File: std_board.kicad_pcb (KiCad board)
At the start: 2 copper layers, 99.1 x 99.1 mm, 191 parts, among them IC1 ESP32, IC2 ACS712, IC3 L78L05, IC4 AMS1117-V, J1 Jumper, J10 J_DHT11, J11 Jumper, J12 Jumper, J13 J_PRess, J14 Jumper, J15 Jumper, J16 J_PRess, J17 Jumper, J18 Jumper, J19 Jumper, J2 Jumper, J22 Jumper, J24 Jumper, J25 Jumper, J26 Jumper, J27 Jumper, J29 Jumper, J3 Jumper, J31 Jumper, J32 Jumper, J33 Jumper, J34 Jumper, J35 Jumper, J36 Jumper, J37 Jumper, J38 Jumper, J39 Jumper, J4 Jumper, J40 Jumper, J41 Jumper, J42 Jumper, J43 Jumper, J44 Jumper, J45 Jumper, J5 Jumper, J6 J_PRess, J7 Jumper, J8 Jumper, J9 Jumper, T1 TRIAC_Micro, T2 TRIAC_Micro, T3 TRIAC_Micro, T4 NPN, T5 NPN, T6 NPN, T7 NPN, T8 PNP, T9 NPN, U1 LNK306

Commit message: TODO list added on REAME.md
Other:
- board text added: "(GPIO12/ADC2_5) L3"
- board text added: "(GPIO14/ADC2_6) L2"
- board text added: "(GPIO21) K3_in"
- board text added: "(GPIO21) T2_in"
- board text added: "(GPIO22) K2_in"
- board text added: "(GPIO23) K1_in"
- board text added: "(GPIO26/ADC2_9) L1"
- board text added: "(GPIO27/ADC2_7) L4"
- board text added: "(GPIO33) T1_in"
- board text added: "(J22)"
- board text added: "(J25)"
- board text added: "(J27)"
- board text added: "(J29)"
- board text added: "(J7)"
- board text added: ".Phase B 220 V or .Neutro 127 V"
- board text added: "AC drive power output"
- board text added: "AC power input or DC voltage on range 7 V < Vin < 30 V"
- board text added: "AC_load_01_out (GPIO21)"
- board text added: "AC_load_02_out (GPIO18)"
- board text added: "AC_load_03_out (GPIO05)"
- board text added: "Current Measure (sensors)"
- board text added: "Digital I/O with Pull-Up"
- board text added: "Phase A"
- board text removed: "AC power input or DC voltage > 7 V"
- board text removed: "AC_Pwr_in_B"
- board text removed: "AC_load_01_out"
- board text removed: "AC_load_02_out"
- board text removed: "AC_load_03_out"
- board text removed: "Inputs (or Outputs)"
- board text removed: "K1_in"
- board text removed: "K2_in"
- board text removed: "K3_in"
- board text removed: "T1_in"
- board text removed: "T2_in"

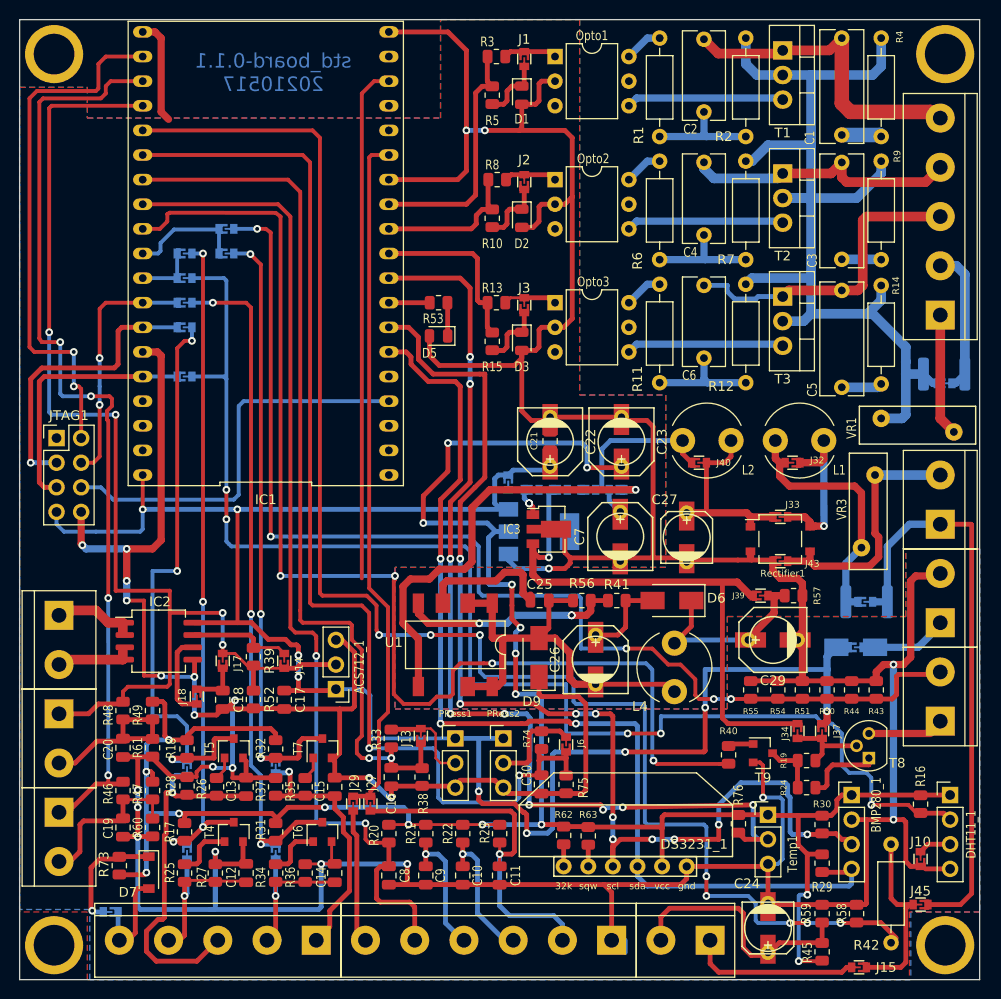
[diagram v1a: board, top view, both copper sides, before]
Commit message: voltage sensor: calculated resistors
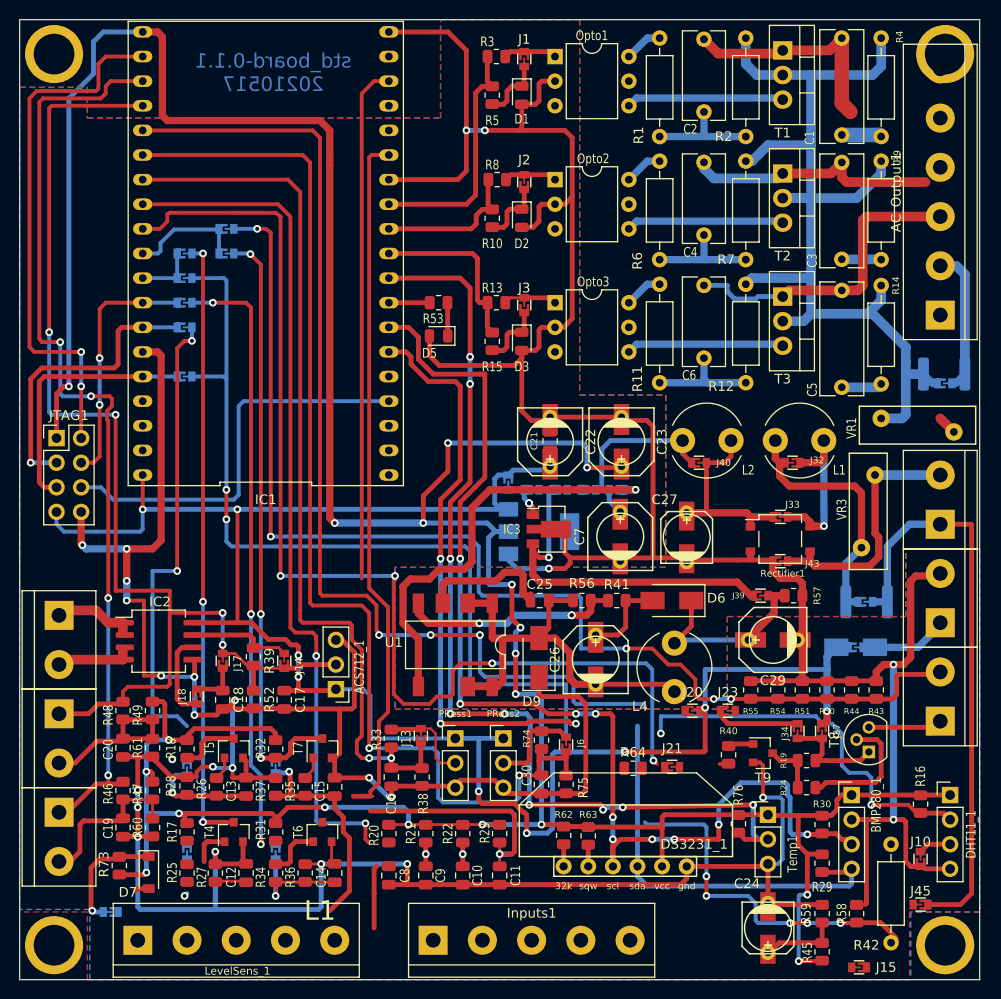
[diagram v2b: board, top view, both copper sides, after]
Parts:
- removed J27, J29: Jumper, thmalmeida:J_0603
- removed Voltimeter_DSO1: Voltimeter, TerminalBlock:TerminalBlock_bornier-2_P5.08mm
- added J20: Jumper, thmalmeida:J_0603, F.Cu at (69.4, 70.0)
- added J21: Jumper, thmalmeida:J_0603, F.Cu at (67.3, 75.8)
- added J23: Jumper, thmalmeida:J_0603, F.Cu at (73.1, 70.0)
- added R64: 220 k, Resistor_SMD:R_0805_2012Metric, F.Cu at (63.3, 76.0)
- AC_Output1: footprint TerminalBlock:TerminalBlock_bornier-5_P5.08mm -> TerminalBlock:TerminalBlock_bornier-6_P5.08mm
- C10, C11, C8, C9: value 100 nF -> 47 nF
- Inputs1: value CONN_6X1 -> CONN_5X1; footprint TerminalBlock:TerminalBlock_bornier-6_P5.08mm -> TerminalBlock:TerminalBlock_bornier-5_P5.08mm
- R19: value 33 k -> 47 k
- R20, R21, R22, R23: value 100 k -> 56 k
- R24: value 1 k -> 2.2 k
- R42: value 500 k -> 470 k
- R58: value 3.3 k -> 3.9 k
- T4, T5, T6, T7, T9: value NPN -> NPN_MMBT222A
- T8: value PNP -> PNP_2N3906
- moved Inputs1 18.4 mm to (42.7, 93.7), turned to 0 degrees
- moved LevelSens_1 18.4 mm to (12.2, 93.7), turned to 0 degrees
- moved T8 0.64 mm to (87.6, 74.3)
- moved R17 0.25 mm to (17.3, 82.5)
- moved R25 0.25 mm to (17.3, 86.8)
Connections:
- AC_Output1 pad 1: /Common -> /Load01
- AC_Output1 pad 2: /Power_AC -> /Load02
- AC_Output1 pad 4: /Load02 -> /Power_AC
- AC_Output1 pad 5: /Load01 -> /Common
- C10 pad 1: /K2_in -> /K3_in
- C11 pad 1: /K3_in -> /T1_in
- C12 pad 1: /L4_probe -> /L1_probe
- C13 pad 1: /L3_probe -> /L2_probe
- C14 pad 1: /L2_probe -> /L3_probe
- C15 pad 1: /L1_probe -> /L4_probe
- C24 pad 1: /Neutro -> Net-(C24-Pad1)
- C8 pad 1: /T1_in -> /K1_in
- C9 pad 1: /K1_in -> /K2_in
- IC1 pad 33: P33 -> /K3_in
- Inputs1 pad 2: /K3_in -> /K1_in
- Inputs1 pad 4: /K1_in -> /K3_in
- J11 pad 1: /L2_in -> /L3_in
- J11 pad 2: /L2_probe -> /L3_probe
- J12 pad 1: /L1_in -> /L4_in
- J12 pad 2: /L1_probe -> /L4_probe
- J15 pad 1: Net-(J15-Pad1) -> /Power_AC_2
- J15 pad 2: /Phase_R -> Net-(J15-Pad2)
- J22 pad 2: /L1_in -> /L4_in
- J25 pad 2: /L2_in -> /L3_in
- J26 pad 2: /L3_in -> /L2_in
- J4 pad 1: /L4_in -> /L1_in
- J4 pad 2: /L4_probe -> /L1_probe
- J45 pad 2: Net-(J15-Pad1) -> Net-(J15-Pad2)
- J5 pad 1: /L3_in -> /L2_in
- J5 pad 2: /L3_probe -> /L2_probe
- J7 pad 2: /L4_in -> /L1_in
- LevelSens_1 pad 1: /L1_probe -> Net-(D7-Pad2)
- LevelSens_1 pad 2: /L2_probe -> /L1_probe
- LevelSens_1 pad 3: /L3_probe -> /L2_probe
- LevelSens_1 pad 4: /L4_probe -> /L3_probe
- LevelSens_1 pad 5: Net-(D7-Pad2) -> /L4_probe
- R17 pad 2: /L4_in -> /L1_in
- R18 pad 2: /L3_in -> /L2_in
- R20 pad 2: /T1_in -> /K1_in
- R21 pad 2: /K1_in -> /K2_in
- R22 pad 2: /K2_in -> /K3_in
- R23 pad 2: /K3_in -> /T1_in
- R25 pad 1: /L4_probe -> /L1_probe
- R26 pad 1: /L3_probe -> /L2_probe
- R27 pad 1: /L4_probe -> /L1_probe
- R28 pad 1: /L3_probe -> /L2_probe
- R31 pad 1: /L2_in -> /L3_in
- R32 pad 1: /L1_in -> /L4_in
- R34 pad 1: /L2_probe -> /L3_probe
- R35 pad 1: /L1_probe -> /L4_probe
- R36 pad 1: /L2_probe -> /L3_probe
- R37 pad 1: /L1_probe -> /L4_probe
- R42 pad 1: Net-(J15-Pad1) -> Net-(J15-Pad2)
- R45 pad 2: /Neutro -> Net-(C24-Pad1)
- R58 pad 2: GND -> Net-(C24-Pad1)
- R59 pad 1: /Neutro -> Net-(C24-Pad1)
- T4 pad 3: /L4_in -> /L1_in
- T5 pad 3: /L3_in -> /L2_in
- T6 pad 3: /L2_in -> /L3_in
- T7 pad 3: /L1_in -> /L4_in
- T8 pad 1: Net-(R24-Pad1) -> Net-(J34-Pad2)
- T8 pad 2: Net-(J34-Pad2) -> Net-(R24-Pad1)
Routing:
- net /+3.3V: track 242.8 -> 358.4 mm, vias 17 -> 19
- net P33: track 71.6 -> 0.00 mm
- net /K3_in: track 37.2 -> 74.1 mm
- net /L3_probe: track 38.3 -> 11.6 mm
- net /Neutro: track 26.1 -> 0.00 mm
- net /L1_probe: track 27.0 -> 3.65 mm
- net Net-(J15-Pad1): track 19.5 -> 0.00 mm
- net /Phase_R: track 17.7 -> 0.00 mm
- net /L2_in: track 71.3 -> 54.0 mm, vias 3 -> 2
- net /K1_in: track 16.2 -> 0.00 mm, vias 1 -> 0
- net /C: track 60.1 -> 46.0 mm
- net /T2_in: track 13.9 -> 0.00 mm
- net /vSensorR: track 157.7 -> 145.7 mm
- net GND: track 573.5 -> 561.9 mm
- net /T1_in: track 106.6 -> 118.0 mm, vias 2 -> 3
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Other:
- board text added: "(GPIO12/ADC2_5) L2"
- board text added: "(GPIO14/ADC2_6) L3"
- board text added: "(GPIO26/ADC2_9) L4"
- board text added: "(GPIO27/ADC2_7) L1"
- board text removed: "(GPIO12/ADC2_5) L3"
- board text removed: "(GPIO14/ADC2_6) L2"
- board text removed: "(GPIO21) T2_in"
- board text removed: "(GPIO26/ADC2_9) L1"
- board text removed: "(GPIO27/ADC2_7) L4"
- board text removed: "(J29)"

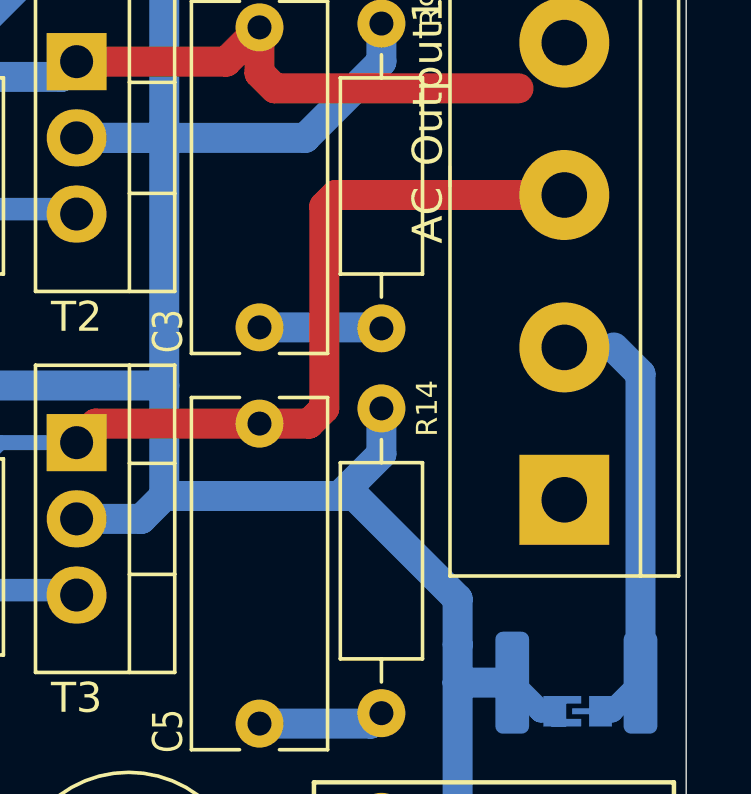
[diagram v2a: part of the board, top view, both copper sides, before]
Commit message: fixed voltage divider of pressure circuit design
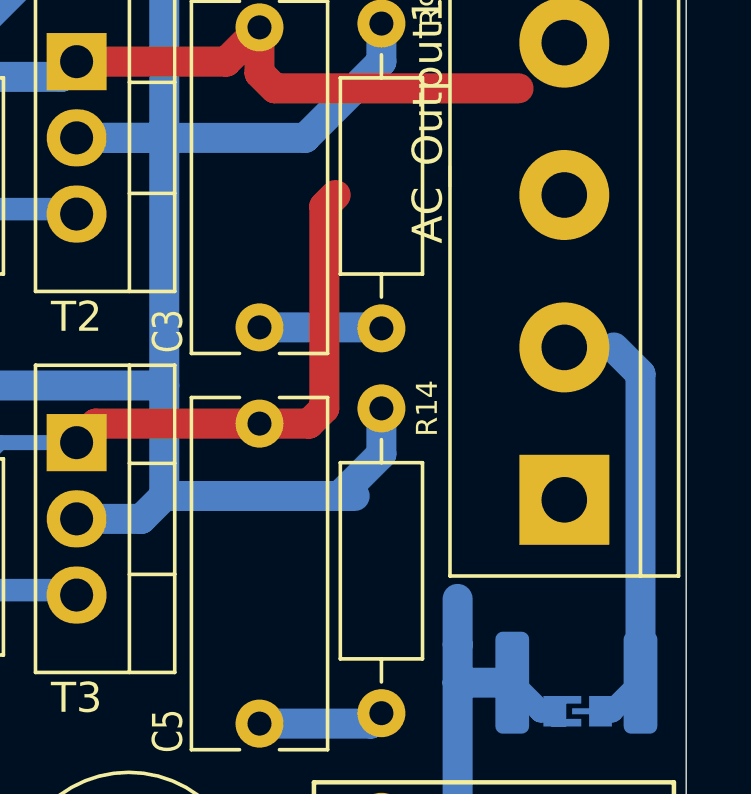
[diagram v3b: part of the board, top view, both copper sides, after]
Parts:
- R42: value 470 k -> 680 k
- R58: value 3.9 k -> 3.3 k
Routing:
- net /Load03: track 32.8 -> 25.2 mm
- net /T1_in: track 118.0 -> 111.5 mm
- net /iSensor2: track 119.6 -> 126.1 mm
- net /Power_AC_2: track 107.7 -> 102.9 mm

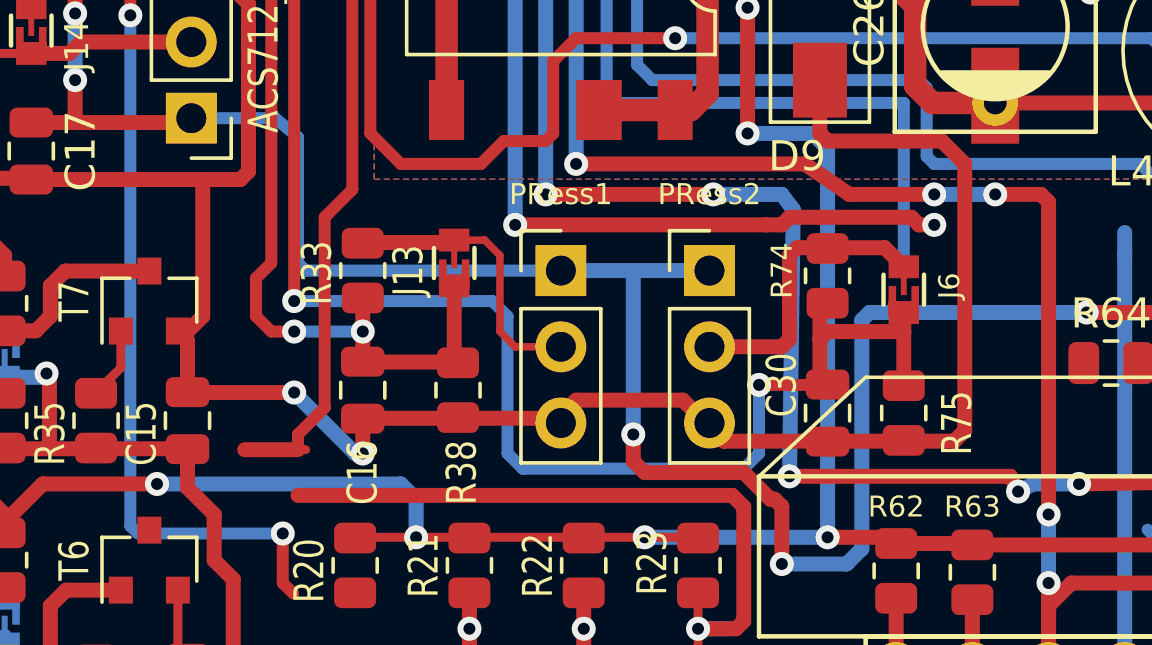
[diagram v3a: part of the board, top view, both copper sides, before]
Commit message: recalculated ADC voltage divider measurement
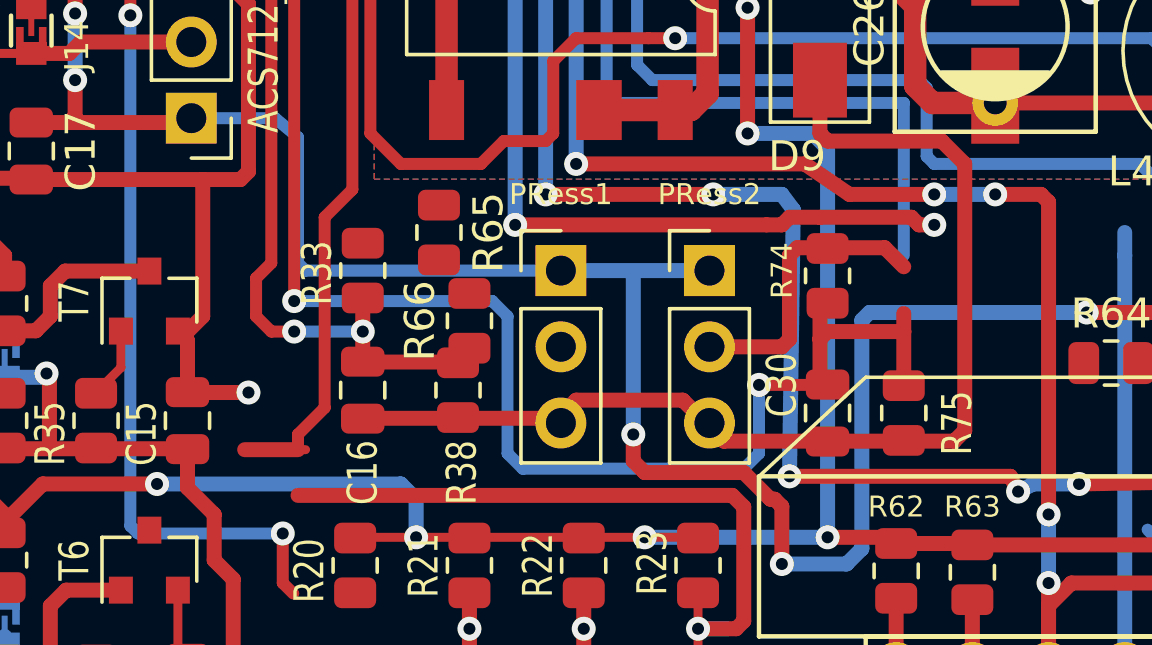
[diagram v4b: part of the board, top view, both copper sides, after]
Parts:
- removed J13, J6: J_PRess, thmalmeida:J_0603
- added R65: 6.8 k, Resistor_SMD:R_0805_2012Metric, F.Cu at (40.9, 71.6)
- added R66: 6.8 k, Resistor_SMD:R_0805_2012Metric, F.Cu at (41.9, 74.6)
- R33, R74: value 120 k -> 12 k
- R38, R75: value 220 k -> 6.8 k
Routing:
- net Net-(PRess1-Pad2): track 9.60 -> 0.00 mm
- net GND: track 561.9 -> 556.1 mm, vias 24 -> 23
- net /PRess_1: track 92.1 -> 89.7 mm
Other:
- board text added: "Pwr_in_1 or 0 V if select some jumpers"
- board text added: "Pwr_in_2 or +5 V if select some jumpers"
- board text removed: "Pwr_in_1"
- board text removed: "Pwr_in_2"
